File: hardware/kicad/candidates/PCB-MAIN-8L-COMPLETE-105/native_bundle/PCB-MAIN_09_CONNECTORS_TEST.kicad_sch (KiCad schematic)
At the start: 18 parts, among them J11 USB4105-GF-A-120, U25 2 channel 0.7 pF USB ESD

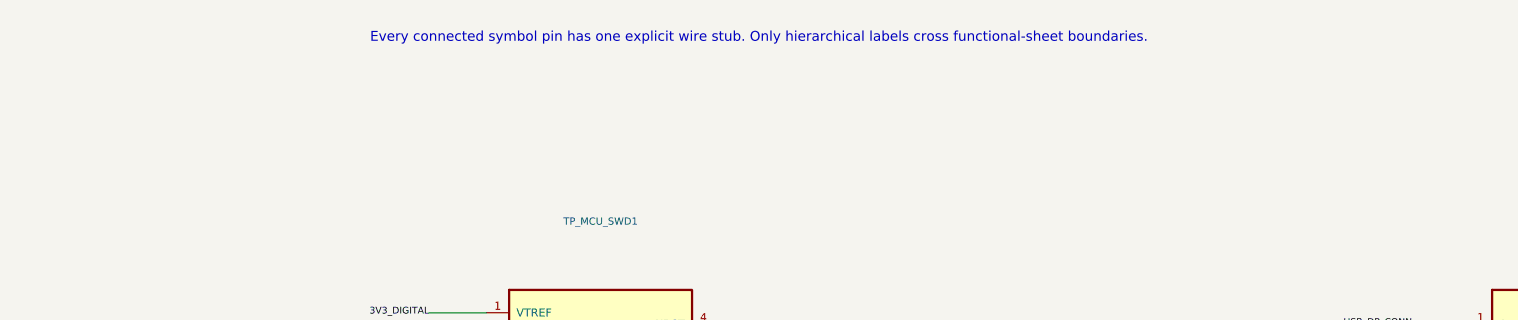
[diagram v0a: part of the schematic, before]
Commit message: PCB-MAIN Rev B: bilingual schematic notes and PDF
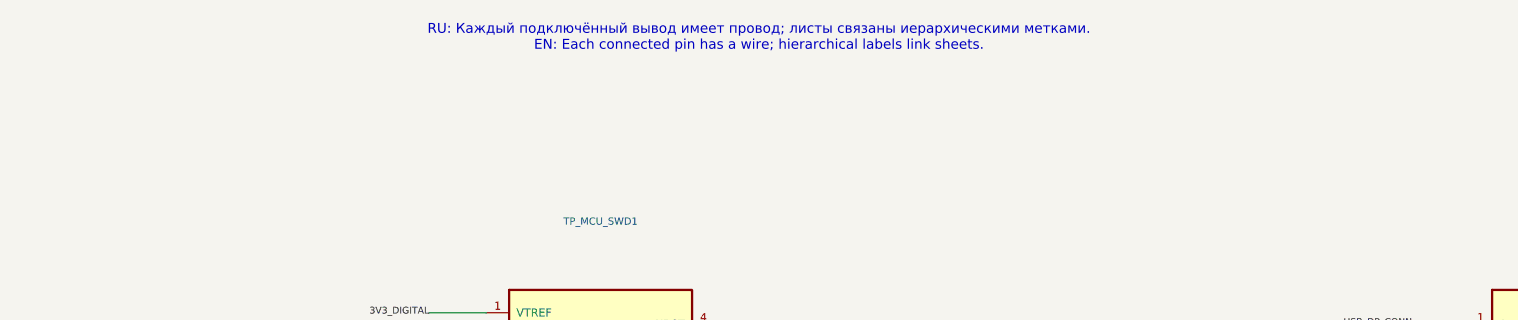
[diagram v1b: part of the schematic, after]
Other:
- note added: "RU: Каждый подключённый вывод имеет провод; листы связаны иерархическими метками. EN: Each connected pin has a wire; hierarchical labels link sheets."
- note removed: "Every connected symbol pin has one explicit wire stub. Only hierarchical labels cross functional-sheet boundaries."
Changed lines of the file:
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@@
     (stroke (width 0.0))
   )
-  (text "Every connected symbol pin has one explicit wire stub. Only hierarchical labels cross functional-sheet boundaries."
+  (text "RU: Каждый подключённый вывод имеет провод; листы связаны иерархическими метками.\nEN: Each connected pin has a wire; hierarchical labels link sheets."
     (at 297.0 12.7 0)
     (effects (font (size 1.1 1.1)))
